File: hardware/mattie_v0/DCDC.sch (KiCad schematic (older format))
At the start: 0 parts

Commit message: dcdc
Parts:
- added C? (x6): 2.2u, Capacitor_SMD:C_0603_1608Metric, symbol Device:C_Small
- added J?: Power, Connector_PinHeader_1.27mm:PinHeader_1x04_P1.27mm_Vertical, symbol Connector:Conn_01x04_Male
- added Q?: DMN2230U, Package_TO_SOT_SMD:SOT-23, symbol Transistor_FET:DMN2230U
- added R?: 10K, Resistor_SMD:R_0603_1608Metric, symbol Device:R_Small
- added U?: MCP1826S-3302, Package_TO_SOT_SMD:SOT-223-3_TabPin2, symbol Regulator_Linear:MCP1826S
- added U?: MCP1826S-1202, Package_TO_SOT_SMD:SOT-223-3_TabPin2, symbol Regulator_Linear:MCP1826S
- added U?: MCP1826T, Package_TO_SOT_SMD:SOT-223-6, symbol favorites:MCP1826T
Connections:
- new net: C?.1, C?.1, Q?.2 (S), U?.1 (VI)
- new net +1V2: C?.1, J?.4 (Pin_4), U?.3 (VO)
- new net +3V3: C?.1, J?.1 (Pin_1), U?.3 (VO)
- new net 5V: C?.1, C?.1, Q?.3 (D), U?.1 (VI)
- new net GND: C?.2, C?.2, C?.2, C?.2, C?.2, C?.2, J?.2 (Pin_2), J?.3 (Pin_3), R?.2, U?.2 (GND), U?.2 (GND)
- new net REG1V2_ON: Q?.1 (G), R?.1
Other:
- note added: "To GPIO on MCU"

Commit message: some tweaks
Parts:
- removed C? (x3): 2.2u, Capacitor_SMD:C_0603_1608Metric, symbol Device:C_Small
- removed Q?: DMN2230U, Package_TO_SOT_SMD:SOT-23, symbol Transistor_FET:DMN2230U
- removed U?: MCP1826S-1202, Package_TO_SOT_SMD:SOT-223-3_TabPin2, symbol Regulator_Linear:MCP1826S
- added C13, C15, C16: 2.2u, Capacitor_SMD:C_0603_1608Metric, symbol Device:C_Small
- added R7, R8: 100K, Resistor_SMD:R_0603_1608Metric, symbol Device:R_Small
- U3: renamed from U?; OrderN (none) -> 579-MCP1826T-1202EDC
- gave numbers to parts that had none: 6
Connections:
- net +1V2: now also U3.4 (VOUT), C16.1
- net +3V3: now also R8.1
- net 5V: now also U3.2 (VIN), C13.1, C15.1
- net GND: now also U3.3 (GND), U3.6 (TAB_GND), C13.2, C15.2, C16.2, R7.2; no longer C12.2, C14.2, C17.2, R6.2, U4.2 (GND)
- net REG1V2_ON: now also U3.1 (NSHDN), R7.1; no longer R6.1
- net PWRGD1V2: now reaches U3.5 (PWRGD)
- net PWRGD1V2: now also R8.2
- new net: C12.2, C14.2, C17.2, U4.2 (GND)
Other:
- note added: "NSHDN - NOT SHUT DOWN (why not call that "enable" ;) \n\n"
- moved on the sheet: R6, U3

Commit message: update
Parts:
- removed R6: 10K, Resistor_SMD:R_0603_1608Metric, symbol Device:R_Small
- added J1: 5V, Connector_PinHeader_2.54mm:PinHeader_1x02_P2.54mm_Vertical, symbol Connector:Conn_01x02_Male
- J3: footprint Connector_PinHeader_1.27mm:PinHeader_1x04_P1.27mm_Vertical -> Connector_PinHeader_2.54mm:PinHeader_1x04_P2.54mm_Vertical
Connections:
- net 5V: now also J1.1 (Pin_1)
- net GND: now also C12.2, C14.2, C17.2, U4.2 (GND), J1.2 (Pin_2)
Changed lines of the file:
@@
 F 0 "J3" V 9154 5462 50  0000 R CNN
 F 1 "Power" V 9063 5462 50  0000 R CNN
-F 2 "Connector_PinHeader_1.27mm:PinHeader_1x04_P1.27mm_Vertical" H 9000 5750 50  0001 C CNN
+F 2 "Connector_PinHeader_2.54mm:PinHeader_1x04_P2.54mm_Vertical" H 9000 5750 50  0001 C CNN
 F 3 "~" H 9000 5750 50  0001 C CNN
 	1    9000 5750
@@
 $EndComp
 $Comp
-L Device:R_Small R?
-U 1 1 5EA0C1DF
-P 1250 4150
-AR Path="/5E994520/5EA0C1DF" Ref="R?"  Part="1"
-AR Path="/5E9881B4/5EA0C1DF" Ref="R?"  Part="1"
-AR Path="/5E988213/5EA0C1DF" Ref="R6"  Part="1"
-F 0 "R6" V 1150 4150 50  0000 C CNN
-F 1 "10K" V 1350 4150 50  0000 C CNN
-F 2 "Resistor_SMD:R_0603_1608Metric" H 1250 4150 50  0001 C CNN
-F 3 "~" H 1250 4150 50  0001 C CNN
-F 4 " 71-CRCW060322R0FKEAC " H 1250 4150 50  0001 C CNN "OrderN"
-	1    1250 4150
-	1    0    0    -1
-$EndComp
+L Connector:Conn_01x02_Male J1
+U 1 1 5EA8DFE6
+P 1650 2800
+F 0 "J1" H 1758 2981 50  0000 C CNN
+F 1 "5V" H 1758 2890 50  0000 C CNN
+F 2 "Connector_PinHeader_2.54mm:PinHeader_1x02_P2.54mm_Vertical" H 1650 2800 50  0001 C CNN
+F 3 "~" H 1650 2800 50  0001 C CNN
+	1    1650 2800
+	1    0    0    -1
+$EndComp
+Text HLabel 2000 2800 2    50   Input ~ 0
+5V
+$Comp
+L power:GND #PWR0113
+U 1 1 5EA52020
+P 3700 3100
+F 0 "#PWR0113" H 3700 2850 50  0001 C CNN
+F 1 "GND" H 3705 2927 50  0000 C CNN
+F 2 "" H 3700 3100 50  0001 C CNN
+F 3 "" H 3700 3100 50  0001 C CNN
+	1    3700 3100
+	1    0    0    -1
+$EndComp
+$Comp
+L power:GND #PWR033
+U 1 1 5EA8F18C
+P 2000 2950
+F 0 "#PWR033" H 2000 2700 50  0001 C CNN
+F 1 "GND" H 2005 2777 50  0000 C CNN
+F 2 "" H 2000 2950 50  0001 C CNN
+F 3 "" H 2000 2950 50  0001 C CNN
+	1    2000 2950
+	1    0    0    -1
+$EndComp
+Wire Wire Line
+	2000 2950 2000 2900
+Wire Wire Line
+	2000 2900 1850 2900
+Wire Wire Line
+	2000 2800 1850 2800
 $EndSCHEMATC

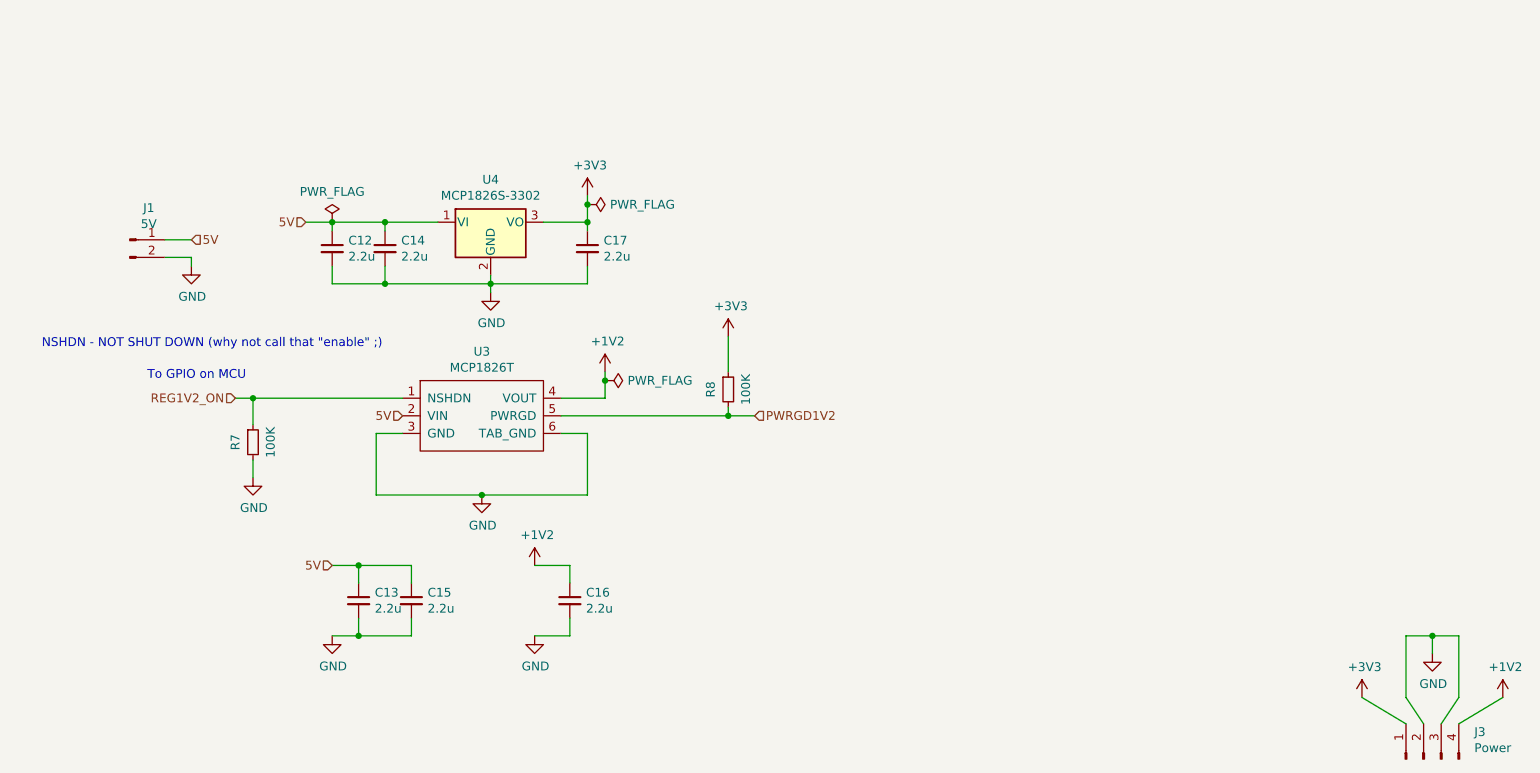
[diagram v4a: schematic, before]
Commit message: added powerswitch for USB power
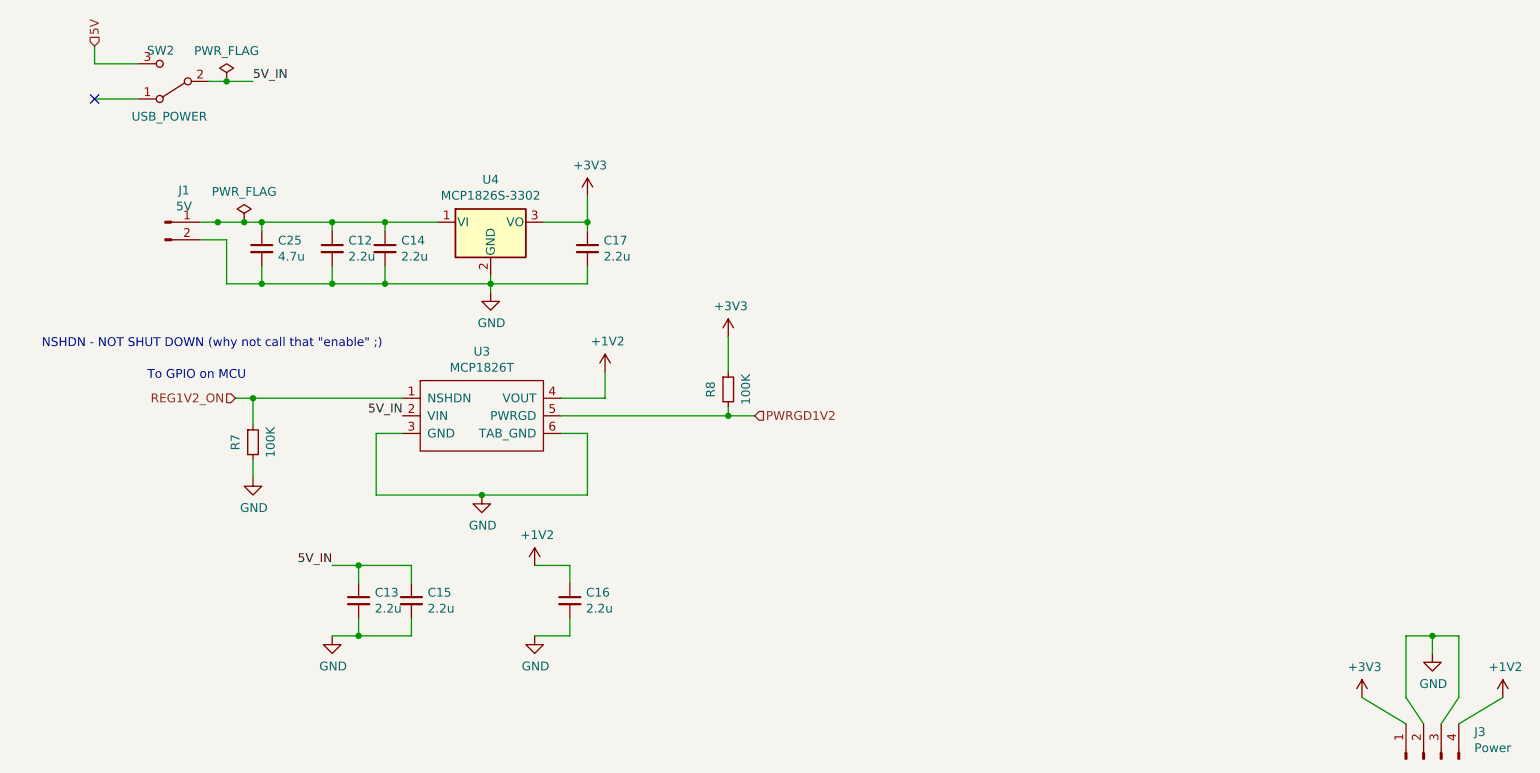
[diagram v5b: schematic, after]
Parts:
- added C25: 4.7u, Capacitor_SMD:C_0603_1608Metric, symbol Device:C_Small
- added SW2: USB_POWER, Button_Switch_SMD:SW_SPDT_PCM12, symbol Switch:SW_SPDT
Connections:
- net 5V: now also SW2.3 (C); no longer C12.1, C13.1, C14.1, C15.1, J1.1 (Pin_1), U3.2 (VIN), U4.1 (VI)
- net GND: now also C25.2
- new net: C12.1, C14.1, C25.1, J1.1 (Pin_1), U4.1 (VI)
- new net 5V_IN: C13.1, C15.1, SW2.2 (B), U3.2 (VIN)
- no-connect marks 0 -> 1
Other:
- moved on the sheet: J1
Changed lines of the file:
@@
 	8900 5050 9050 5050
 Connection ~ 9050 5050
-Text HLabel 2650 2700 0    50   Input ~ 0
-5V
-$Comp
-L power:PWR_FLAG #FLG0101
-U 1 1 5E9E8811
-P 2800 2700
-F 0 "#FLG0101" H 2800 2775 50  0001 C CNN
-F 1 "PWR_FLAG" H 2800 2873 50  0000 C CNN
-F 2 "" H 2800 2700 50  0001 C CNN
-F 3 "~" H 2800 2700 50  0001 C CNN
-	1    2800 2700
-	1    0    0    -1
-$EndComp
 $Comp
 L Regulator_Linear:MCP1826S U4
@@
 	1    0    0    -1
 $EndComp
-Wire Wire Line
-	4250 2700 4250 2600
 Connection ~ 4250 2700
-$Comp
-L power:PWR_FLAG #FLG0102
-U 1 1 5E9F395D
-P 4250 2600
-F 0 "#FLG0102" H 4250 2675 50  0001 C CNN
-F 1 "PWR_FLAG" V 4250 2728 50  0000 L CNN
-F 2 "" H 4250 2600 50  0001 C CNN
-F 3 "~" H 4250 2600 50  0001 C CNN
-	1    4250 2600
-	0    1    1    0
-$EndComp
-Connection ~ 4250 2600
-Wire Wire Line
-	4250 2600 4250 2550
 Wire Wire Line
 	4350 3700 4100 3700
@@
 	1    0    0    -1
 $EndComp
-Wire Wire Line
-	4350 3700 4350 3600
-$Comp
-L power:PWR_FLAG #FLG0103
-U 1 1 5E9F74F1
-P 4350 3600
-F 0 "#FLG0103" H 4350 3675 50  0001 C CNN
-F 1 "PWR_FLAG" V 4350 3728 50  0000 L CNN
-F 2 "" H 4350 3600 50  0001 C CNN
-F 3 "~" H 4350 3600 50  0001 C CNN
-	1    4350 3600
-	0    1    1    0
-$EndComp
-Connection ~ 4350 3600
-Wire Wire Line
-	4350 3600 4350 3550
 Text HLabel 2250 3700 0    50   Input ~ 0
 REG1V2_ON
@@
 Wire Wire Line
 	4100 3800 5050 3800
-Wire Wire Line
-	2650 2700 2800 2700
 Connection ~ 2800 2700
 Connection ~ 3100 2700
-Text HLabel 3200 3800 0    50   Input ~ 0
-5V
 $Comp
 L Device:C_Small C?
@@
 	1    0    0    -1
 $EndComp
-Text HLabel 2800 4650 0    50   Input ~ 0
-5V
 $Comp
 L power:GND #PWR0109
@@
 L Connector:Conn_01x02_Male J1
 U 1 1 5EA8DFE6
-P 1650 2800
-F 0 "J1" H 1758 2981 50  0000 C CNN
-F 1 "5V" H 1758 2890 50  0000 C CNN
-F 2 "Connector_PinHeader_2.54mm:PinHeader_1x02_P2.54mm_Vertical" H 1650 2800 50  0001 C CNN
-F 3 "~" H 1650 2800 50  0001 C CNN
-	1    1650 2800
-	1    0    0    -1
-$EndComp
-Text HLabel 2000 2800 2    50   Input ~ 0
-5V
+P 1850 2700
+F 0 "J1" H 1958 2881 50  0000 C CNN
+F 1 "5V" H 1958 2790 50  0000 C CNN
+F 2 "Connector_PinHeader_2.54mm:PinHeader_1x02_P2.54mm_Vertical" H 1850 2700 50  0001 C CNN
+F 3 "~" H 1850 2700 50  0001 C CNN
+	1    1850 2700
+	1    0    0    -1
+$EndComp
 $Comp
 L power:GND #PWR0113
@@
 	1    0    0    -1
 $EndComp
-$Comp
-L power:GND #PWR033
-U 1 1 5EA8F18C
-P 2000 2950
-F 0 "#PWR033" H 2000 2700 50  0001 C CNN
-F 1 "GND" H 2005 2777 50  0000 C CNN
-F 2 "" H 2000 2950 50  0001 C CNN
-F 3 "" H 2000 2950 50  0001 C CNN
-	1    2000 2950
-	1    0    0    -1
-$EndComp
-Wire Wire Line
-	2000 2950 2000 2900
-Wire Wire Line
-	2000 2900 1850 2900
-Wire Wire Line
-	2000 2800 1850 2800
+Wire Wire Line
+	2200 2800 2050 2800
+Text HLabel 1450 1700 1    50   Input ~ 0
+5V
+Wire Wire Line
+	1700 2000 1450 2000
+Wire Wire Line
+	1450 1800 1450 1700
+$Comp
+L Switch:SW_SPDT SW?
+U 1 1 5EA4044B
+P 1900 1900
+AR Path="/5E994520/5EA4044B" Ref="SW?"  Part="1"
+AR Path="/5E9881B4/5EA4044B" Ref="SW?"  Part="1"
+AR Path="/5E988213/5EA4044B" Ref="SW2"  Part="1"
+F 0 "SW2" H 1975 1725 50  0000 C CNN
+F 1 "USB_POWER" H 1925 2100 50  0000 C CNN
+F 2 "Button_Switch_SMD:SW_SPDT_PCM12" H 1900 1900 50  0001 C CNN
+F 3 "~" H 1900 1900 50  0001 C CNN
+F 4 "401-2016-1-ND " H 1900 1900 50  0001 C CNN "OrderN"
+	1    1900 1900
+	-1   0    0    1
+$EndComp
+Wire Wire Line
+	1700 1800 1450 1800
+Wire Wire Line
+	2400 3050 2400 2950
+$Comp
+L Device:C_Small C?
+U 1 1 5EA4045C
+P 2400 2850
+AR Path="/5E994520/5EA4045C" Ref="C?"  Part="1"
+AR Path="/5E9881B4/5EA4045C" Ref="C?"  Part="1"
+AR Path="/5E988213/5EA4045C" Ref="C25"  Part="1"
+F 0 "C25" H 2492 2896 50  0000 L CNN
+F 1 "4.7u" H 2492 2805 50  0000 L CNN
+F 2 "Capacitor_SMD:C_0603_1608Metric" H 2400 2850 50  0001 C CNN
+F 3 "~" H 2400 2850 50  0001 C CNN
+F 4 " 346-CM105X5R475M25AT " H 2400 2850 50  0001 C CNN "OrderN"
+	1    2400 2850
+	1    0    0    -1
+$EndComp
+NoConn ~ 1450 2000
+Text Label 3200 3800 2    50   ~ 0
+5V_IN
+Text Label 2800 4650 2    50   ~ 0
+5V_IN
+Text Label 2350 1900 0    50   ~ 0
+5V_IN
+Wire Wire Line
+	2050 2700 2150 2700
+Wire Wire Line
+	2400 2750 2400 2700
+Connection ~ 2400 2700
+Wire Wire Line
+	2400 2700 2800 2700
+Wire Wire Line
+	2800 3050 2400 3050
+Connection ~ 2800 3050
+Wire Wire Line
+	2400 3050 2200 3050
+Wire Wire Line
+	2200 2800 2200 3050
+Connection ~ 2400 3050
+Wire Wire Line
+	2100 1900 2200 1900
+$Comp
+L power:PWR_FLAG #FLG0101
+U 1 1 5EA83F67
+P 2200 1900
+F 0 "#FLG0101" H 2200 1975 50  0001 C CNN
+F 1 "PWR_FLAG" H 2200 2073 50  0000 C CNN
+F 2 "" H 2200 1900 50  0001 C CNN
+F 3 "~" H 2200 1900 50  0001 C CNN
+	1    2200 1900
+	1    0    0    -1
+$EndComp
+Connection ~ 2200 1900
+Wire Wire Line
+	2200 1900 2350 1900
+$Comp
+L power:PWR_FLAG #FLG0104
+U 1 1 5EA84231
+P 2300 2700
+F 0 "#FLG0104" H 2300 2775 50  0001 C CNN
+F 1 "PWR_FLAG" H 2300 2873 50  0000 C CNN
+F 2 "" H 2300 2700 50  0001 C CNN
+F 3 "~" H 2300 2700 50  0001 C CNN
+	1    2300 2700
+	1    0    0    -1
+$EndComp
+Connection ~ 2150 2700
+Wire Wire Line
+	2150 2700 2300 2700
+Connection ~ 2300 2700
+Wire Wire Line
+	2300 2700 2400 2700
+Wire Wire Line
+	4250 2550 4250 2700
+Wire Wire Line
+	4350 3550 4350 3700
 $EndSCHEMATC

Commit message: adding some cap
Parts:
- added C26: 0.1u, Capacitor_SMD:C_0603_1608Metric, symbol Device:C_Small
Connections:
- net +1V2: now also C26.2
- net 5V_IN: now also C12.1, C14.1, C25.1, J1.1 (Pin_1), U4.1 (VI)
- net GND: now also C26.1
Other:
- moved on the sheet: J1
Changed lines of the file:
@@
 L Connector:Conn_01x02_Male J1
 U 1 1 5EA8DFE6
-P 1850 2700
-F 0 "J1" H 1958 2881 50  0000 C CNN
-F 1 "5V" H 1958 2790 50  0000 C CNN
-F 2 "Connector_PinHeader_2.54mm:PinHeader_1x02_P2.54mm_Vertical" H 1850 2700 50  0001 C CNN
-F 3 "~" H 1850 2700 50  0001 C CNN
-	1    1850 2700
+P 1600 2700
+F 0 "J1" H 1708 2881 50  0000 C CNN
+F 1 "5V" H 1708 2790 50  0000 C CNN
+F 2 "Connector_PinHeader_2.54mm:PinHeader_1x02_P2.54mm_Vertical" H 1600 2700 50  0001 C CNN
+F 3 "~" H 1600 2700 50  0001 C CNN
+	1    1600 2700
 	1    0    0    -1
 $EndComp
@@
 $EndComp
 Wire Wire Line
-	2200 2800 2050 2800
+	2200 2800 1800 2800
 Text HLabel 1450 1700 1    50   Input ~ 0
 5V
@@
 5V_IN
 Wire Wire Line
-	2050 2700 2150 2700
-Wire Wire Line
 	2400 2750 2400 2700
 Connection ~ 2400 2700
@@
 	1    0    0    -1
 $EndComp
-Connection ~ 2150 2700
-Wire Wire Line
-	2150 2700 2300 2700
 Connection ~ 2300 2700
 Wire Wire Line
@@
 Wire Wire Line
 	4350 3550 4350 3700
+Wire Wire Line
+	1800 2700 2300 2700
+$Comp
+L Device:C_Small C?
+U 1 1 5EA1D6AA
+P 4600 4850
+AR Path="/5E9881B4/5EA1D6AA" Ref="C?"  Part="1"
+AR Path="/5E98823A/5EA1D6AA" Ref="C?"  Part="1"
+AR Path="/5E988213/5EA1D6AA" Ref="C26"  Part="1"
+F 0 "C26" V 4371 4850 50  0000 C CNN
+F 1 "0.1u" V 4462 4850 50  0000 C CNN
+F 2 "Capacitor_SMD:C_0603_1608Metric" H 4600 4850 50  0001 C CNN
+F 3 "~" H 4600 4850 50  0001 C CNN
+F 4 " 963-TMK107BJ104KA-T " H 4600 4850 50  0001 C CNN "Mouser"
+	1    4600 4850
+	-1   0    0    1
+$EndComp
+Wire Wire Line
+	4600 4750 4600 4650
+Wire Wire Line
+	4600 4650 4150 4650
+Connection ~ 4150 4650
+Wire Wire Line
+	4600 4950 4600 5050
+Wire Wire Line
+	4600 5050 4150 5050
+Connection ~ 4150 5050
+Text Label 2000 2700 1    50   ~ 0
+5V_IN
 $EndSCHEMATC
